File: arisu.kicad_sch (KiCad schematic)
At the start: 8 parts

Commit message: Schematic mostly finished
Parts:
- removed H1, H2, H3, H4, H5, H6, H7, H8: MountingHole, Mounting_Holes:MountingHole_2.2mm_M2_Pad, symbol Mechanical:MountingHole
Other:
- note added: "TODO: keep in mind: plate keycaps height usb C LEDS holes probably desirable"

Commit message: Some layout
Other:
- note added: "TODO: keep in mind: plate keycaps height usb C LEDS holes probably desirable SWD header"
- note removed: "TODO: keep in mind: plate keycaps height usb C LEDS holes probably desirable"
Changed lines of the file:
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@@
     (stroke (width 0) (type default) (color 0 0 0 0))
   )
-  (text "TODO:\nkeep in mind: plate\nkeycaps height\nusb C\nLEDS\nholes probably desirable"
+  (text "TODO:\nkeep in mind: plate\nkeycaps height\nusb C\nLEDS\nholes probably desirable\nSWD header"
     (at 85.09 26.67 0)
     (effects (font (size 1.27 1.27)) (justify left bottom))

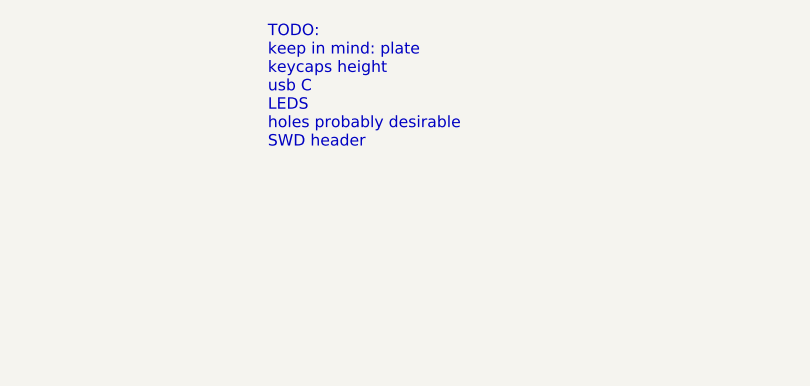
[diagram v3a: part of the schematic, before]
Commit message: Finished layout (for now), board outline, and new trrs jacks
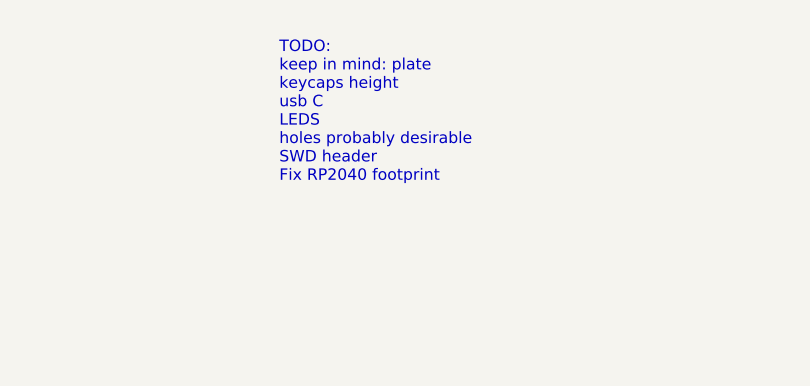
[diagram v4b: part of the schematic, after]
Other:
- note added: "TODO: keep in mind: plate keycaps height usb C LEDS holes probably desirable SWD header Fix RP2040 footprint"
- note removed: "TODO: keep in mind: plate keycaps height usb C LEDS holes probably desirable SWD header"
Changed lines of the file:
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@@
     (stroke (width 0) (type default) (color 0 0 0 0))
   )
-  (text "TODO:\nkeep in mind: plate\nkeycaps height\nusb C\nLEDS\nholes probably desirable\nSWD header"
-    (at 85.09 26.67 0)
+  (text "TODO:\nkeep in mind: plate\nkeycaps height\nusb C\nLEDS\nholes probably desirable\nSWD header\nFix RP2040 footprint\n"
+    (at 86.36 30.48 0)
     (effects (font (size 1.27 1.27)) (justify left bottom))
   )
@@
     )
     (path "/8c4379f0-6f5f-4ee8-9db5-ef285281fc90/9d758cb0-626c-430f-812f-9b31179a836b"
-      (reference "J1") (unit 1) (value "35RASMT5CHNTRX") (footprint "arisu-split:35RASMT5CHNTRX")
+      (reference "J1") (unit 1) (value "SJ-43514-SMT-TR") (footprint "arisu-split:SJ-43514-SMT-TR")
     )
     (path "/e3cb8eae-e69f-4e9c-8f54-e476a90f2f61/c4645a3c-368a-4151-97c2-8de92003f6f9"
@@
     )
     (path "/8c4379f0-6f5f-4ee8-9db5-ef285281fc90/f3affb04-9997-4ea7-a23c-90048e0c4fad"
-      (reference "J3") (unit 1) (value "35RASMT5CHNTRX") (footprint "arisu-split:35RASMT5CHNTRX")
+      (reference "J3") (unit 1) (value "SJ-43514-SMT-TR") (footprint "arisu-split:SJ-43514-SMT-TR")
     )
     (path "/e3cb8eae-e69f-4e9c-8f54-e476a90f2f61/55f1188c-73db-482b-a907-ad87045211a0"

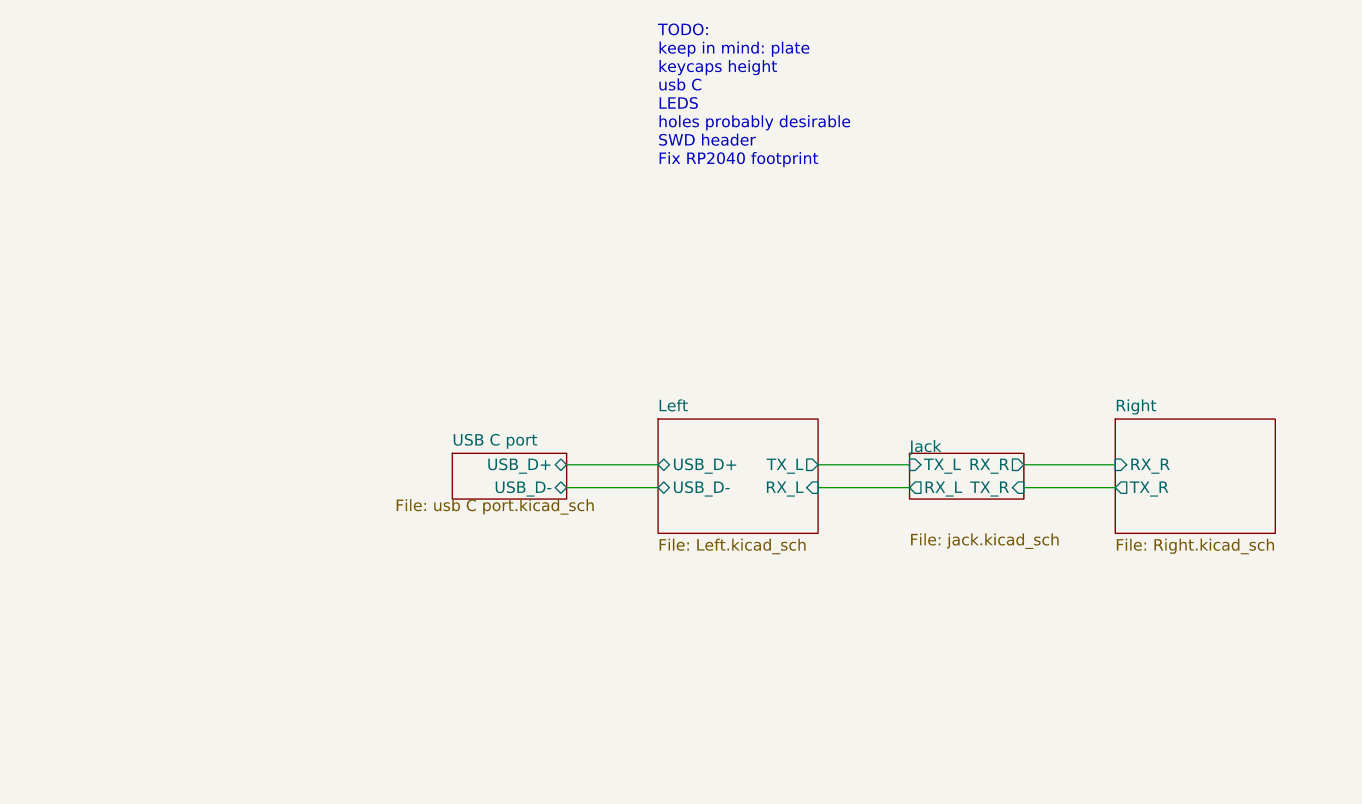
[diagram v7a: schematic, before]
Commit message: left side of keyboard finished for the time being
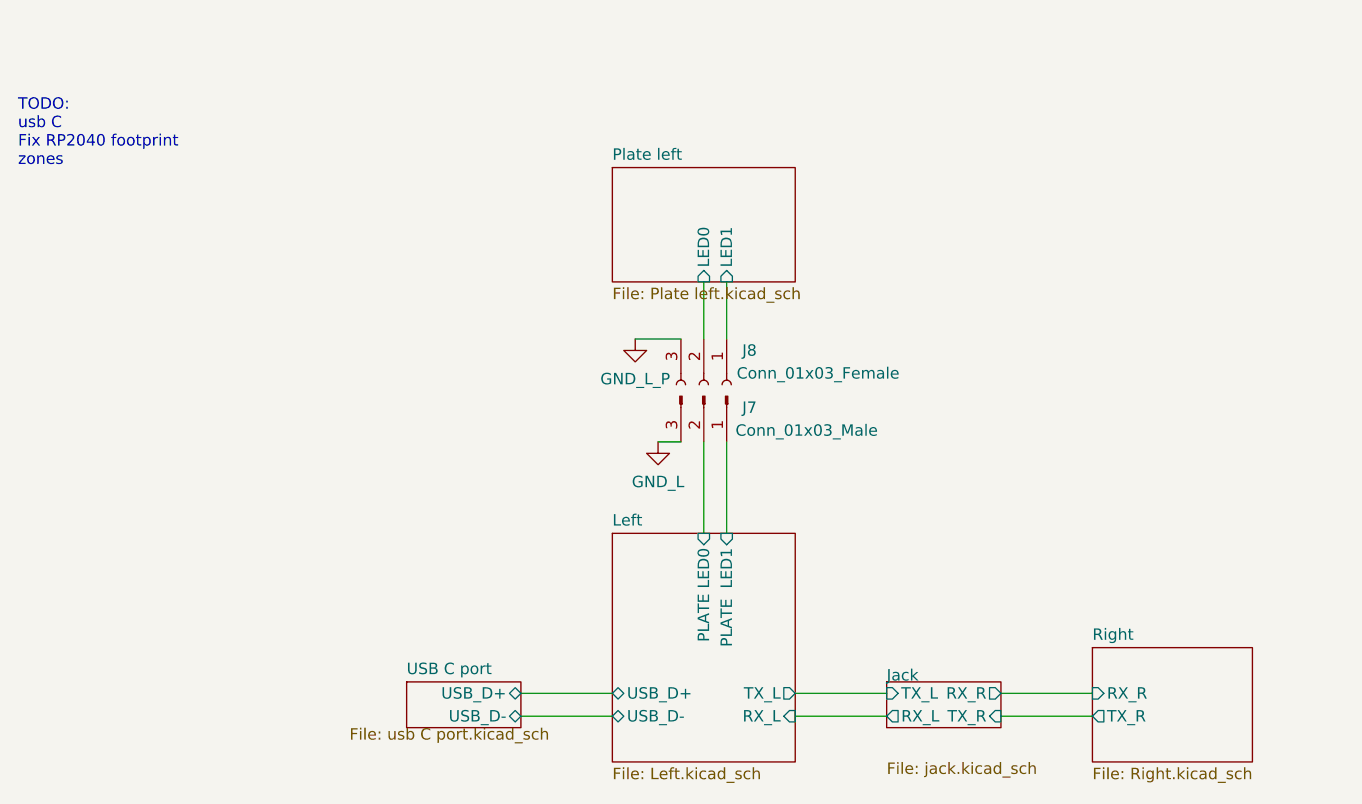
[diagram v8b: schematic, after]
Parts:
- added J7: Conn_01x03_Male, Connector_PinHeader_1.27mm:PinHeader_1x03_P1.27mm_Horizontal, symbol Connector:Conn_01x03_Male
- added J8: Conn_01x03_Female, arisu-split:Pads 1.27mm, symbol Connector:Conn_01x03_Female
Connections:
- new net GND_L: J7.3 (Pin_3)
- new net GND_L_P: J8.3 (Pin_3)
- new net Left/PLATE  LED1: J7.1 (Pin_1)
- new net Left/PLATE LED0: J7.2 (Pin_2)
- new net Plate left/LED0: J8.2 (Pin_2)
- new net Plate left/LED1: J8.1 (Pin_1)
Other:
- added sheet Plate left (Plate left.kicad_sch)
- sheet Left ports: added PLATE  LED1, PLATE LED0; removed none
- note added: "TODO: usb C Fix RP2040 footprint zones"
- note removed: "TODO: keep in mind: plate keycaps height usb C LEDS holes probably desirable SWD header Fix RP2040 footprint"
